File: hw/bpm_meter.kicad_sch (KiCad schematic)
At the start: 24 parts, among them J1 Conn_01x03_Pin, Q1 AO3400A, Q2 AO3400A, U1 SLS0391FR1A1GD, U2 AOZ1282CI

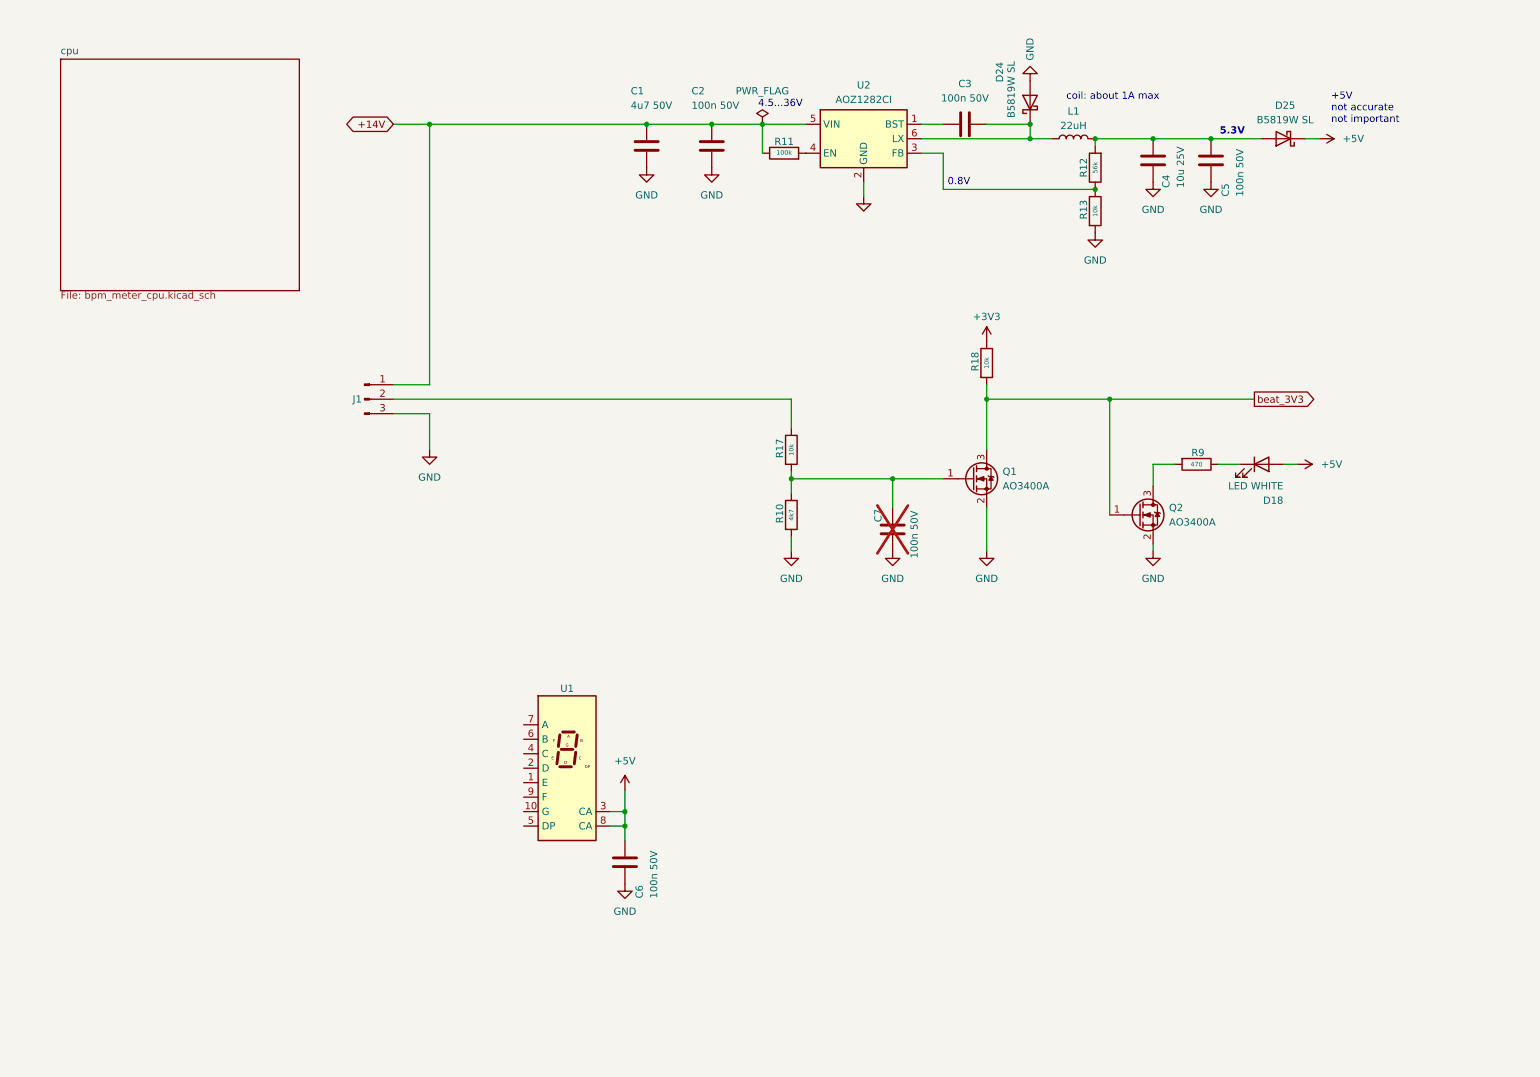
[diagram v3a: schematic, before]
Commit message: Added H11L1 optocoupler to library and schematic
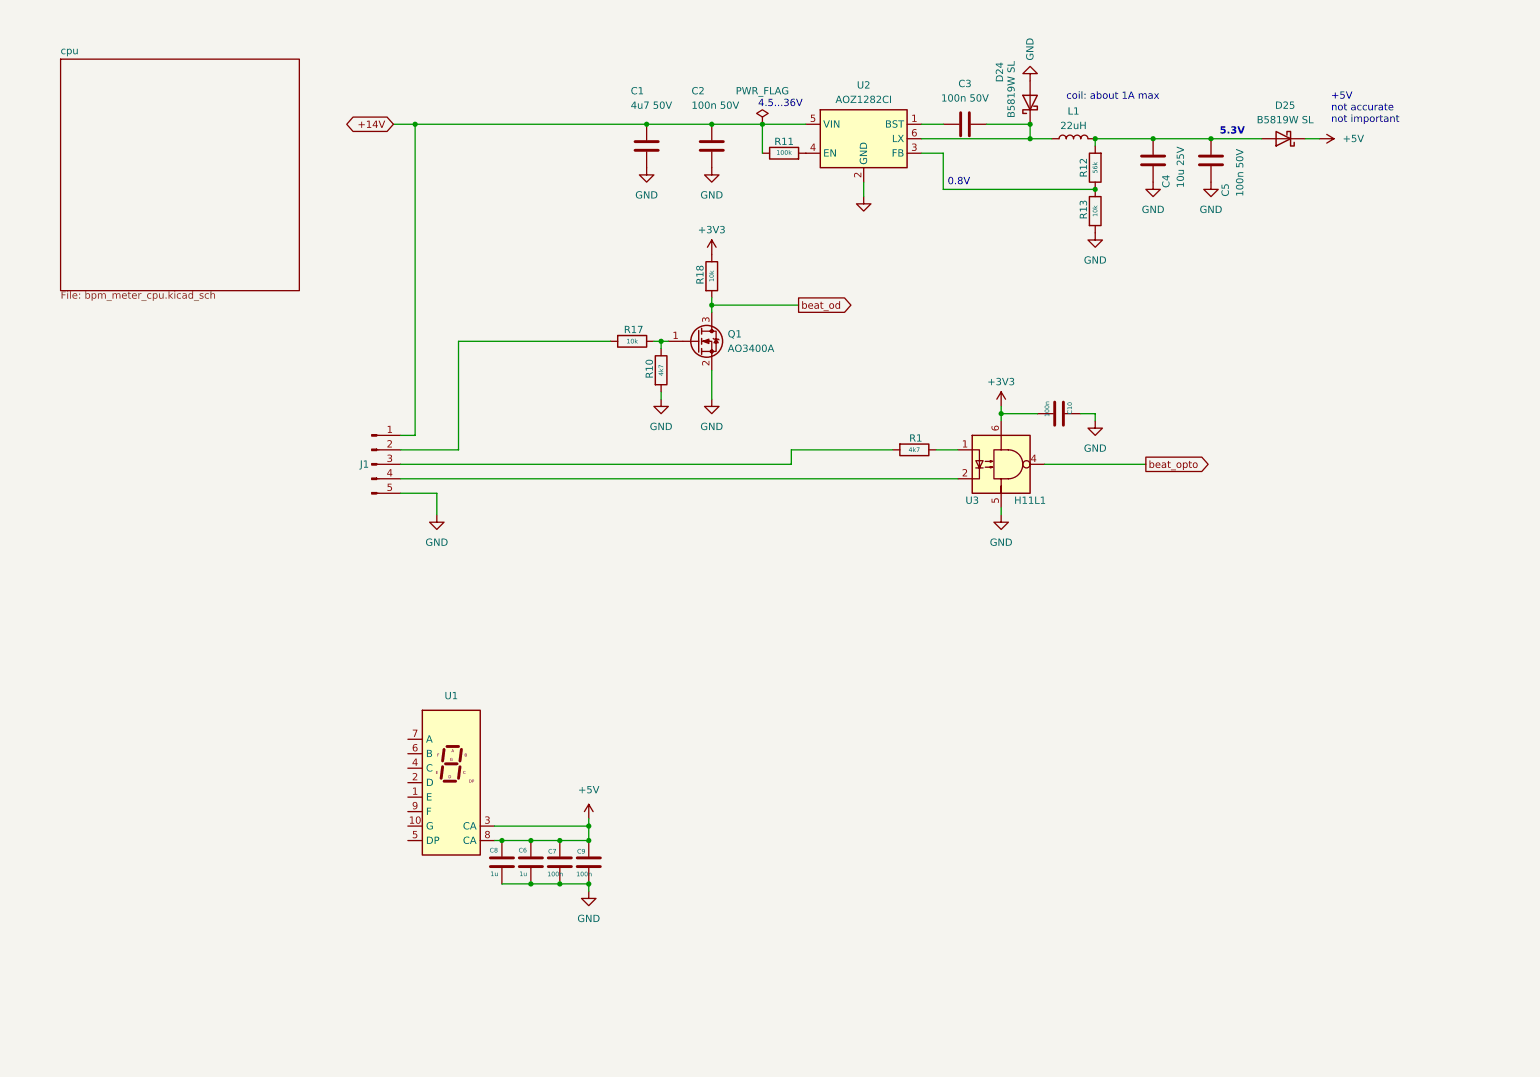
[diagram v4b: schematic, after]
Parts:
- removed C6, C7: 100n 50V, Diode_SMD:D_0805_2012Metric, symbol Device:C
- removed D18: LED WHITE, 00_project_library:LED_0603_1608Metric, symbol 00_project_library:LED WHITE
- removed Q2: AO3400A, Package_TO_SOT_SMD:SOT-23, symbol Transistor_FET:AO3400A
- removed R9: 470, Resistor_SMD:R_0402_1005Metric_Pad0.72x0.64mm_HandSolder, symbol Device:R
- removed U1: SLS0391FR1A1GD, Display_7Segment:KCSC02-105, symbol Display_Character:KCSA02-105
- added C10, C7, C9: 100n, Capacitor_SMD:C_0402_1005Metric, symbol 00_project_library:C
- added C6, C8: 1u, Capacitor_SMD:C_0402_1005Metric, symbol 00_project_library:C
- added R1: 4k7, Resistor_SMD:R_0402_1005Metric_Pad0.72x0.64mm_HandSolder, symbol Device:R
- added U1: SLS0391FR1A1GD, 00_project_library:SLS0391, symbol 00_project_library:SLS0391FR1A1GD
- added U3: H11L1, 00_project_library:SOP-6-2.54mm, symbol Isolator:H11L1
- J1: symbol Connector:Conn_01x03_Pin -> Connector:Conn_01x05_Pin
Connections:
- net +3V3: now also C10.2, U3.6
- net +5V: now also C6.1, C7.1, C8.1, C9.1, U1.3 (CA), U1.8 (CA)
- net GND: now also J1.5 (Pin_5), C10.1, C6.2, C7.2, C8.2, C9.2, U3.5; no longer J1.3 (Pin_3)
- net at R17.1: now also Q1.1 (G), R10.1; no longer J1.2 (Pin_2)
- net beat_3V3 renamed beat_od
- new net: J1.2 (Pin_2), R17.2
- new net: R1.1, U3.1
- new net: J1.4 (Pin_4), U3.2
- new net: J1.3 (Pin_3), R1.2
- new net beat_opto: U3.4
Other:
- moved on the sheet: Q1, R10, R17, R18

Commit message: Connected the segment displays using dual FETs
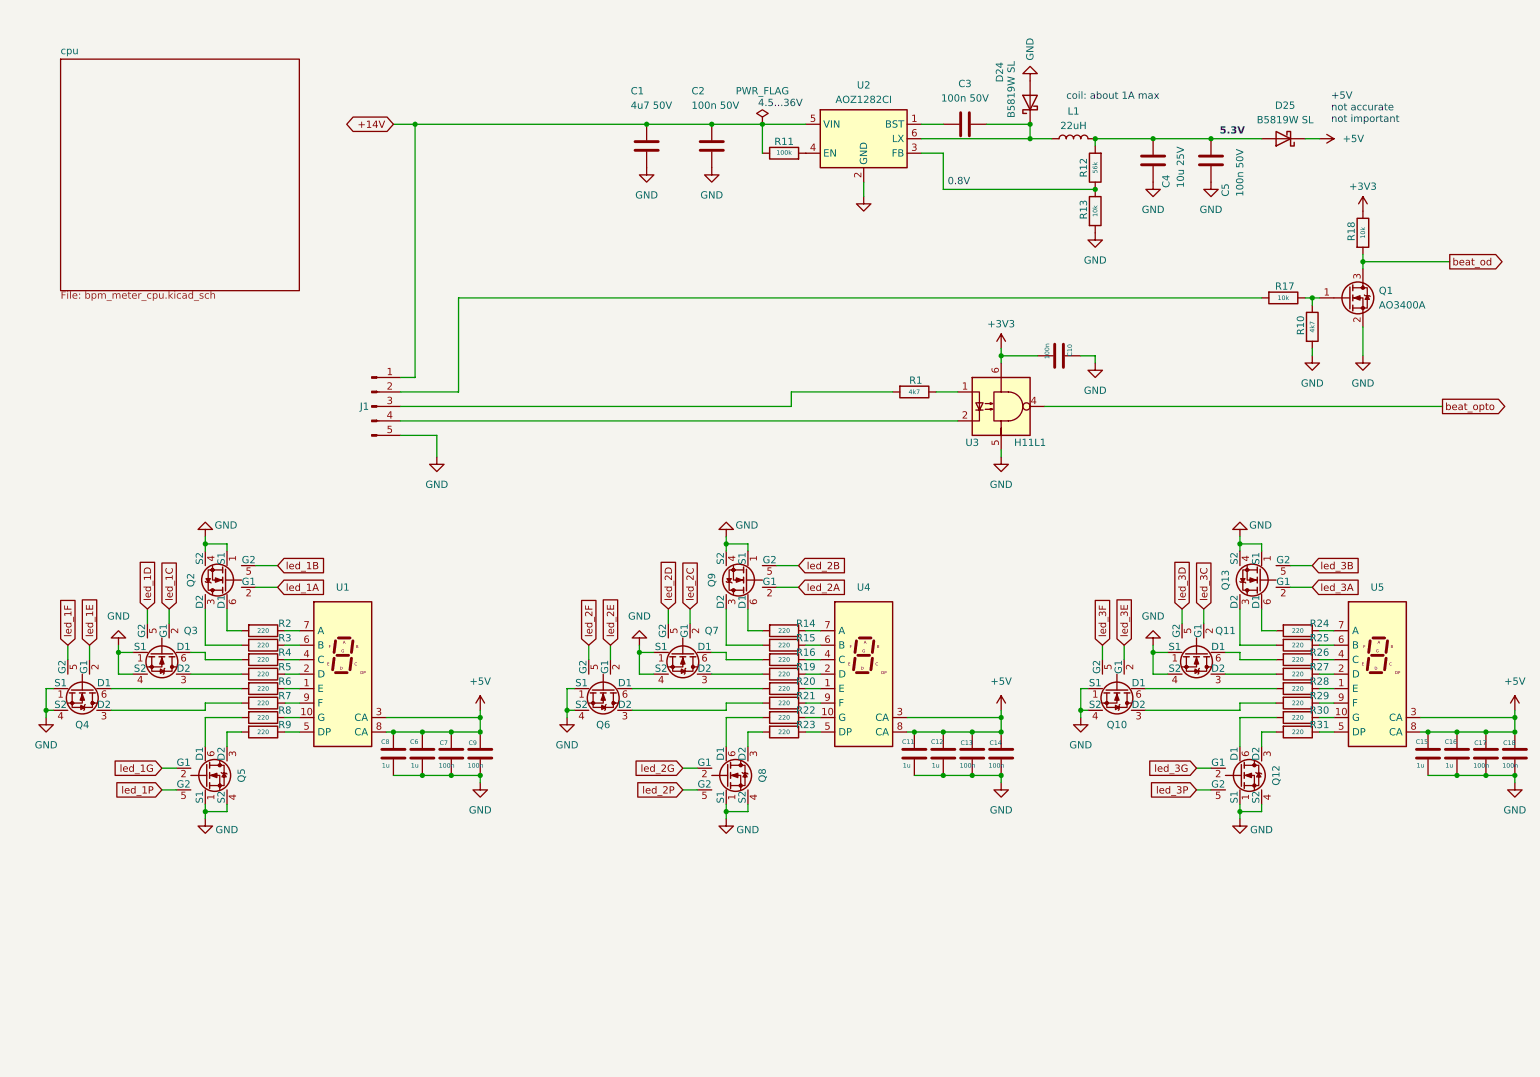
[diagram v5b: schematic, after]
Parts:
- added C11, C12, C15, C16: 1u, Capacitor_SMD:C_0402_1005Metric, symbol 00_project_library:C
- added C13, C14, C17, C18: 100n, Capacitor_SMD:C_0402_1005Metric, symbol 00_project_library:C
- added Q10, Q11, Q12, Q13, Q2, Q3, Q4, Q5, Q6, Q7, Q8, Q9: DMN2004VK, Package_TO_SOT_SMD:SOT-563, symbol 00_project_library:DMN60H080DS
- added R14, R15, R16, R19, R2, R20, R21, R22, R23, R24, R25, R26, R27, R28, R29, R3, R30, R31, R4, R5, R6, R7, R8, R9: 220, Resistor_SMD:R_0402_1005Metric_Pad0.72x0.64mm_HandSolder, symbol Device:R
- added U4, U5: SLS0391FR1A1GD, 00_project_library:SLS0391, symbol 00_project_library:SLS0391FR1A1GD
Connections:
- net +5V: now also C11.1, C12.1, C13.1, C14.1, C15.1, C16.1, C17.1, C18.1, U4.3 (CA), U4.8 (CA), U5.3 (CA), U5.8 (CA)
- net GND: now also C11.2, C12.2, C13.2, C14.2, C15.2, C16.2, C17.2, C18.2, Q10.1 (S1), Q10.4 (S2), Q11.1 (S1), Q11.4 (S2), Q12.1 (S1), Q12.4 (S2), Q13.1 (S1), Q13.4 (S2), Q2.1 (S1), Q2.4 (S2), Q3.1 (S1), Q3.4 (S2), Q4.1 (S1), Q4.4 (S2), Q5.1 (S1), Q5.4 (S2), Q6.1 (S1), Q6.4 (S2), Q7.1 (S1), Q7.4 (S2), Q8.1 (S1), Q8.4 (S2), Q9.1 (S1), Q9.4 (S2)
- net at U1.1 (E): now also R6.1
- net at U1.10 (G): now also R8.1
- net at U1.2 (D): now also R5.1
- net at U1.4 (C): now also R4.1
- net at U1.5 (DP): now also R9.1
- net at U1.6 (B): now also R3.1
- net at U1.7 (A): now also R2.1
- net at U1.9 (F): now also R7.1
- new net: Q2.3 (D2), R3.2
- new net: Q2.6 (D1), R2.2
- new net: Q12.3 (D2), R31.2
- new net: Q12.6 (D1), R30.2
- new net: R16.1, U4.4 (C)
- new net: Q7.6 (D1), R16.2
- new net: R21.1, U4.9 (F)
- new net: Q6.3 (D2), R21.2
- new net: Q9.3 (D2), R15.2
- new net: Q9.6 (D1), R14.2
- new net: Q10.3 (D2), R29.2
- new net: Q10.6 (D1), R28.2
- new net: Q4.3 (D2), R7.2
- new net: R24.1, U5.7 (A)
- new net: Q13.6 (D1), R24.2
- new net: R30.1, U5.10 (G)
- new net: R28.1, U5.1 (E)
- new net: R27.1, U5.2 (D)
- new net: R26.1, U5.4 (C)
- new net: R31.1, U5.5 (DP)
- new net: R25.1, U5.6 (B)
- new net: R29.1, U5.9 (F)
- new net: Q4.6 (D1), R6.2
- new net: Q3.6 (D1), R4.2
- new net: Q11.3 (D2), R27.2
- new net: Q11.6 (D1), R26.2
- new net: R14.1, U4.7 (A)
- new net: R19.1, U4.2 (D)
- new net: Q7.3 (D2), R19.2
- new net: Q5.3 (D2), R9.2
- new net: R20.1, U4.1 (E)
- new net: Q6.6 (D1), R20.2
- new net: R15.1, U4.6 (B)
- new net: Q3.3 (D2), R5.2
- new net: Q13.3 (D2), R25.2
- new net: Q8.3 (D2), R23.2
- new net: Q8.6 (D1), R22.2
- new net: R22.1, U4.10 (G)
- new net: R23.1, U4.5 (DP)
- new net: Q5.6 (D1), R8.2
- new net led_1A: Q2.2 (G1)
- new net led_1B: Q2.5 (G2)
- new net led_1C: Q3.2 (G1)
- new net led_1D: Q3.5 (G2)
- new net led_1E: Q4.2 (G1)
- new net led_1F: Q4.5 (G2)
- new net led_1G: Q5.2 (G1)
- new net led_1P: Q5.5 (G2)
- new net led_2A: Q9.2 (G1)
- new net led_2B: Q9.5 (G2)
- new net led_2C: Q7.2 (G1)
- new net led_2D: Q7.5 (G2)
- new net led_2E: Q6.2 (G1)
- new net led_2F: Q6.5 (G2)
- new net led_2G: Q8.2 (G1)
- new net led_2P: Q8.5 (G2)
- new net led_3A: Q13.2 (G1)
- new net led_3B: Q13.5 (G2)
- new net led_3C: Q11.2 (G1)
- new net led_3D: Q11.5 (G2)
- new net led_3E: Q10.2 (G1)
- new net led_3F: Q10.5 (G2)
- new net led_3G: Q12.2 (G1)
- new net led_3P: Q12.5 (G2)
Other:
- moved on the sheet: C10, C6, C7, C8, C9, J1, Q1, R1, R10, R17, R18, U1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

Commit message: Export to PCB
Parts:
- J1: footprint Connector_PinHeader_2.54mm:PinHeader_1x03_P2.54mm_Vertical -> Connector_PinHeader_2.54mm:PinHeader_1x05_P2.54mm_Vertical
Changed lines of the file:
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@@
       (effects (font (size 1.27 1.27)) hide)
     )
-    (property "Footprint" "Connector_PinHeader_2.54mm:PinHeader_1x03_P2.54mm_Vertical" (at 78.74 81.28 0)
+    (property "Footprint" "Connector_PinHeader_2.54mm:PinHeader_1x05_P2.54mm_Vertical" (at 78.74 81.28 0)
       (effects (font (size 1.27 1.27)) hide)
     )
